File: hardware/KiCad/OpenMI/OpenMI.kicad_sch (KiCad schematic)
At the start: 11 parts, among them Q1 MASTERGAN1, Q2 Q_NMOS_DGS, Q3 Q_NMOS_DGS

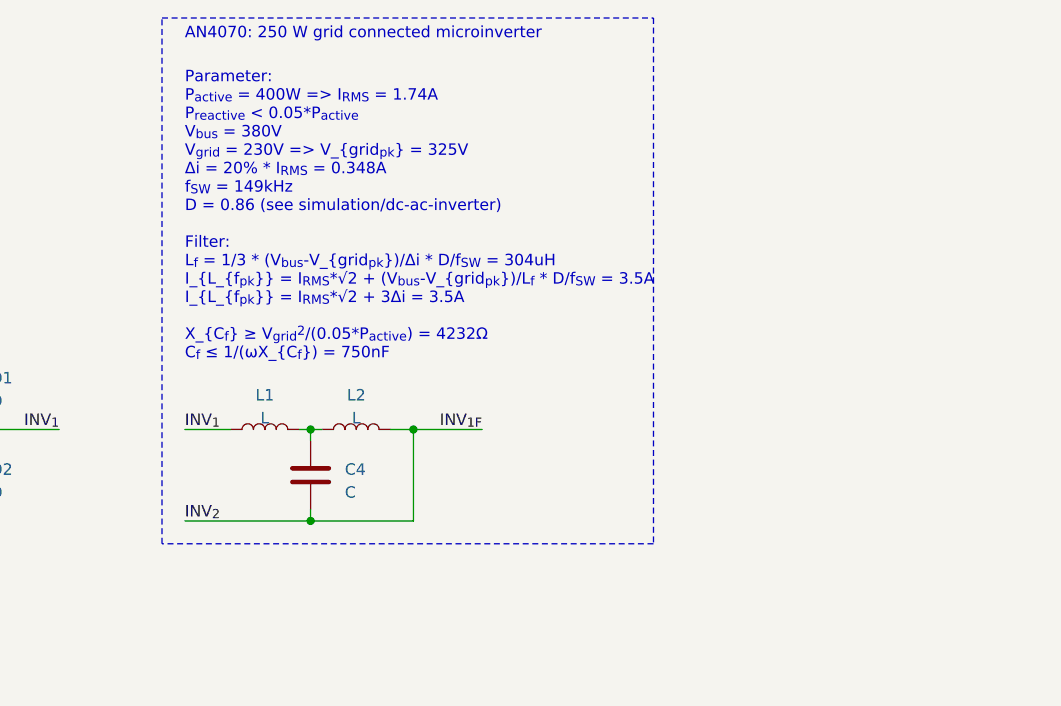
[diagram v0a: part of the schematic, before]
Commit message: hw: Add some possible inductors
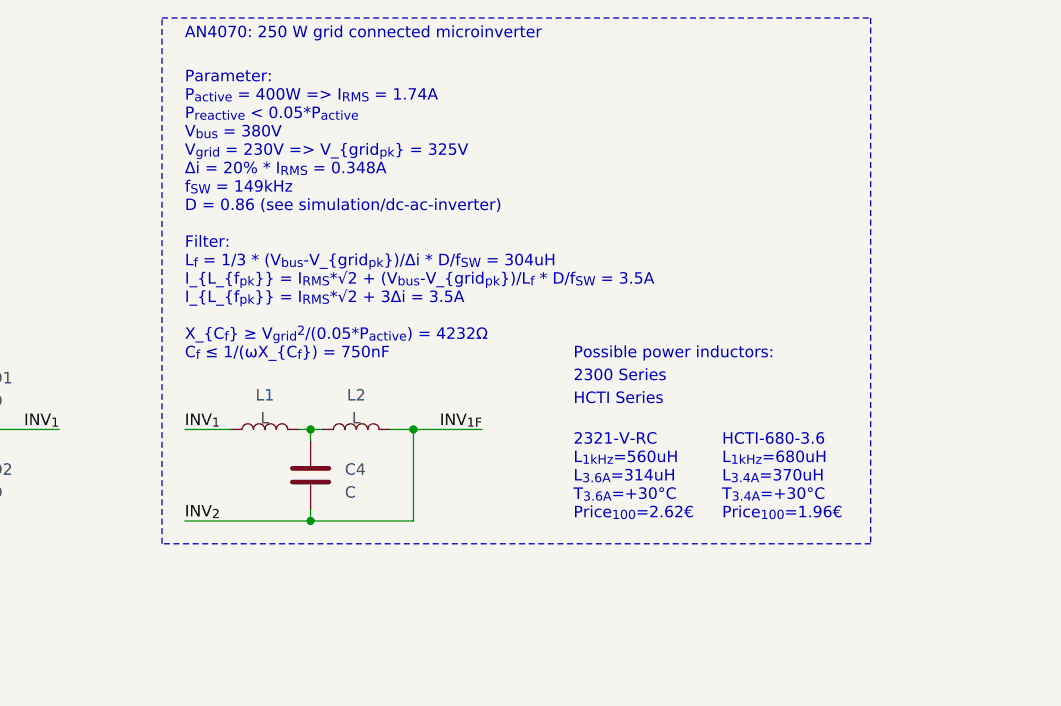
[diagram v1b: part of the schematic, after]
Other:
- note added: "2300 Series"
- note added: "2321-V-RC L_{1kHz}=560uH L_{3.6A}=314uH T_{3.6A}=+30°C Price_{100}=2.62€"
- note added: "HCTI Series"
- note added: "HCTI-680-3.6 L_{1kHz}=680uH L_{3.4A}=370uH T_{3.4A}=+30°C Price_{100}=1.96€"
- note added: "Possible power inductors:"
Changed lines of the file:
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@@
     (stroke (width 0) (type default))
   )
-  (rectangle (start 115.57 26.67) (end 170.18 85.09)
+  (rectangle (start 115.57 26.67) (end 194.31 85.09)
     (stroke (width 0) (type dash))
     (fill (type none))
+  )
+  (text "Possible power inductors:" (at 161.29 64.77 0)
+    (effects (font (size 1.27 1.27)) (justify left bottom))
+  )
+  (text "2321-V-RC \nL_{1kHz}=560uH\nL_{3.6A}=314uH\nT_{3.6A}=+30°C\nPrice_{100}=2.62€"
+    (at 161.29 82.55 0)
+    (effects (font (size 1.27 1.27)) (justify left bottom))
   )
   (text "AN4070: 250 W grid connected microinverter" (at 118.11 29.21 0)
     (effects (font (size 1.27 1.27)) (justify left bottom) (href "https://www.st.com/resource/en/application_note/dm00050692-250-w-grid-connected-microinverter-stmicroelectronics.pdf"))
   )
+  (text "HCTI-680-3.6\nL_{1kHz}=680uH\nL_{3.4A}=370uH\nT_{3.4A}=+30°C\nPrice_{100}=1.96€"
+    (at 177.8 82.55 0)
+    (effects (font (size 1.27 1.27)) (justify left bottom))
+  )
+  (text "HCTI Series" (at 161.29 69.85 0)
+    (effects (font (size 1.27 1.27)) (justify left bottom) (href "https://eu.mouser.com/datasheet/2/643/ds-st-high-current-torodial-inductors-series-1661536.pdf"))
+  )
+  (text "2300 Series" (at 161.29 67.31 0)
+    (effects (font (size 1.27 1.27)) (justify left bottom) (href "https://eu.mouser.com/datasheet/2/54/2300_series-776044.pdf"))
+  )
   (text "Parameter:\nP_{active} = 400W => I_{RMS} = 1.74A\nP_{reactive} < 0.05*P_{active}\nV_{bus} = 380V\nV_{grid} = 230V => V_{grid_{pk}} = 325V\nΔi = 20% * I_{RMS} = 0.348A\nf_{SW} = 149kHz\nD = 0.86 (see simulation/dc-ac-inverter)\n\nFilter:\nL_{f} = 1/3 * (V_{bus}-V_{grid_{pk}})/Δi * D/f_{SW} = 304uH\nI_{L_{f_{pk}}} = I_{RMS}*√2 + (V_{bus}-V_{grid_{pk}})/L_{f} * D/f_{SW} = 3.5A\nI_{L_{f_{pk}}} = I_{RMS}*√2 + 3Δi = 3.5A\n\nX_{C_{f}} ≥ V_{grid}^{2}/(0.05*P_{active}) = 4232Ω\nC_{f} ≤ 1/(ωX_{C_{f}}) = 750nF"

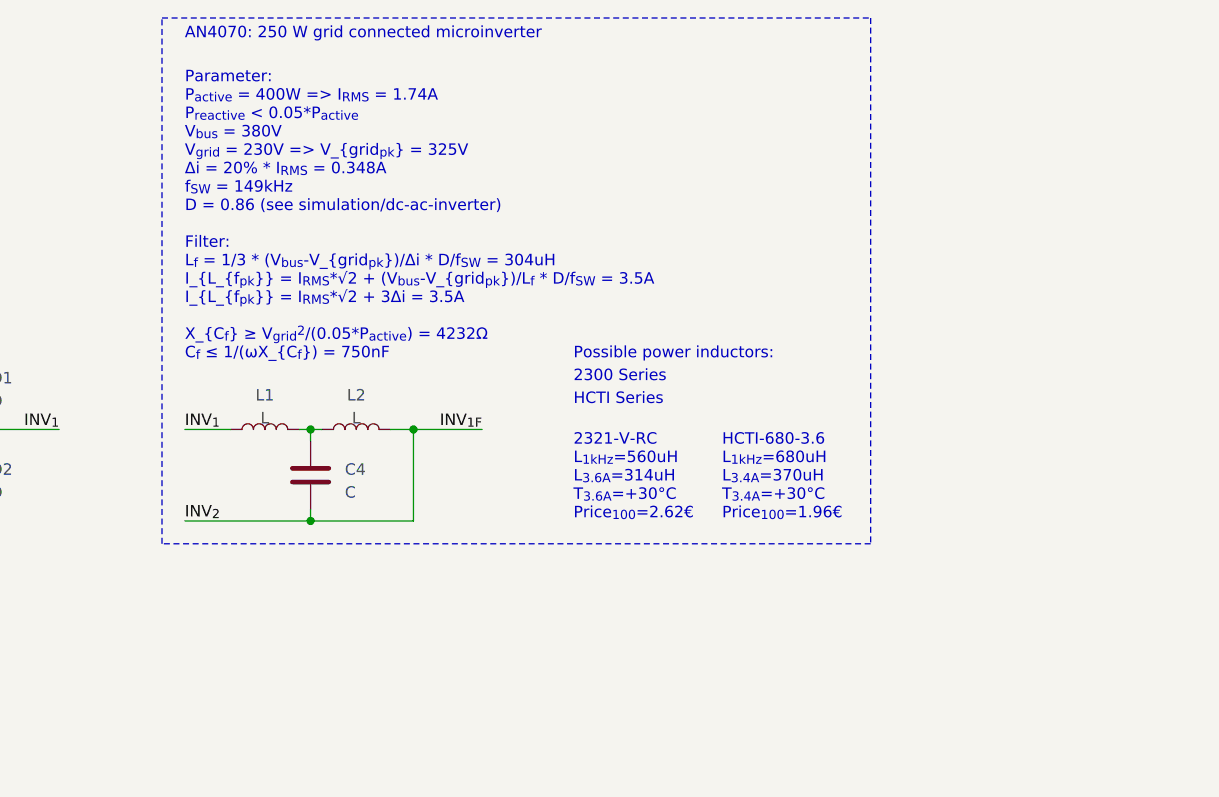
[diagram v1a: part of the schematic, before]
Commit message: hw: fix switching frequency -> update required filter inductance
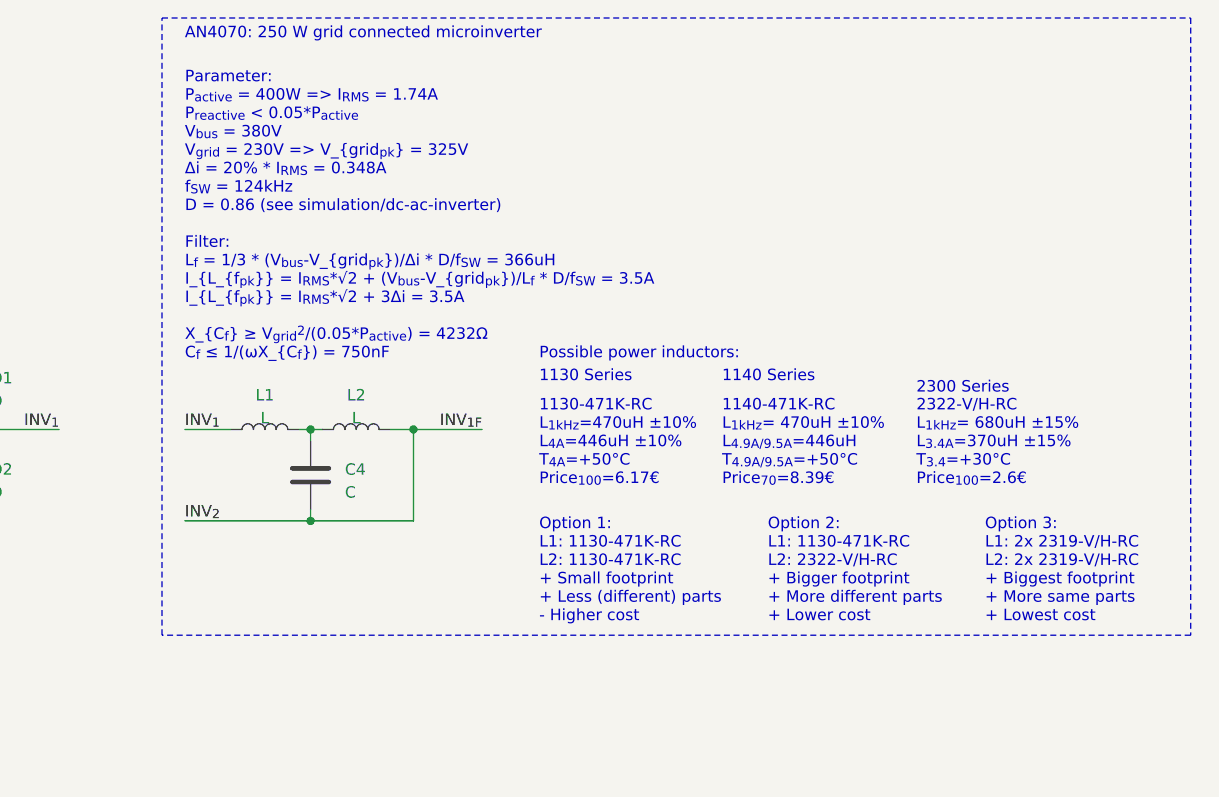
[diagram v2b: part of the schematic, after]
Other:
- note added: "1130 Series"
- note added: "1130-471K-RC L_{1kHz}=470uH ±10% L_{4A}=446uH ±10% T_{4A}=+50°C Price_{100}=6.17€"
- note added: "1140 Series"
- note added: "1140-471K-RC L_{1kHz}= 470uH ±10% L_{4.9A/9.5A}=446uH T_{4.9A/9.5A}=+50°C Price_{70}=8.39€"
- note added: "2322-V/H-RC L_{1kHz}= 680uH ±15% L_{3.4A}=370uH ±15% T_{3.4}=+30°C Price_{100}=2.6€"
- note added: "Option 1: L1: 1130-471K-RC L2: 1130-471K-RC + Small footprint + Less (different) parts - Higher cost"
- note added: "Option 2: L1: 1130-471K-RC L2: 2322-V/H-RC + Bigger footprint + More different parts + Lower cost"
- note added: "Option 3: L1: 2x 2319-V/H-RC L2: 2x 2319-V/H-RC + Biggest footprint + More same parts + Lowest cost"
- note added: "Parameter: P_{active} = 400W => I_{RMS} = 1.74A P_{reactive} < 0.05*P_{active} V_{bus} = 380V V_{grid} = 230V => V_{grid_{pk}} = 325V Δi = 20% * I_{RMS} = 0.348A f_{SW} = 124kHz D = 0.86 (see simulation/dc-ac-inverter) Filter: L_{f} = 1/3 * (V_{bus}-V_{grid_{pk}})/Δi * D/f_{SW} = 366uH I_{L_{f_{pk}}} = I_{RMS}*√2 + (V_{bus}-V_{grid_{pk}})/L_{f} * D/f_{SW} = 3.5A I_{L_{f_{pk}}} = I_{RMS}*√2 + 3Δi 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"
- note removed: "2321-V-RC L_{1kHz}=560uH L_{3.6A}=314uH T_{3.6A}=+30°C Price_{100}=2.62€"
- note removed: "HCTI Series"
- note removed: "HCTI-680-3.6 L_{1kHz}=680uH L_{3.4A}=370uH T_{3.4A}=+30°C Price_{100}=1.96€"
- note removed: "Parameter: P_{active} = 400W => I_{RMS} = 1.74A P_{reactive} < 0.05*P_{active} V_{bus} = 380V V_{grid} = 230V => V_{grid_{pk}} = 325V Δi = 20% * I_{RMS} = 0.348A f_{SW} = 149kHz D = 0.86 (see simulation/dc-ac-inverter) Filter: L_{f} = 1/3 * (V_{bus}-V_{grid_{pk}})/Δi * D/f_{SW} = 304uH I_{L_{f_{pk}}} = I_{RMS}*√2 + (V_{bus}-V_{grid_{pk}})/L_{f} * D/f_{SW} = 3.5A I_{L_{f_{pk}}} = I_{RMS}*√2 + 3Δi 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"
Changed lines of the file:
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@@
     (stroke (width 0) (type default))
   )
-  (rectangle (start 115.57 26.67) (end 194.31 85.09)
+  (rectangle (start 115.57 26.67) (end 229.87 95.25)
     (stroke (width 0) (type dash))
     (fill (type none))
   )
-  (text "Possible power inductors:" (at 161.29 64.77 0)
+  (text "Option 1:\nL1: 1130-471K-RC\nL2: 1130-471K-RC\n+ Small footprint\n+ Less (different) parts\n- Higher cost"
+    (at 157.48 93.98 0)
     (effects (font (size 1.27 1.27)) (justify left bottom))
   )
-  (text "2321-V-RC \nL_{1kHz}=560uH\nL_{3.6A}=314uH\nT_{3.6A}=+30°C\nPrice_{100}=2.62€"
-    (at 161.29 82.55 0)
+  (text "Possible power inductors:" (at 157.48 64.77 0)
+    (effects (font (size 1.27 1.27)) (justify left bottom))
+  )
+  (text "1130-471K-RC \nL_{1kHz}=470uH ±10%\nL_{4A}=446uH ±10%\nT_{4A}=+50°C\nPrice_{100}=6.17€"
+    (at 157.48 78.74 0)
     (effects (font (size 1.27 1.27)) (justify left bottom))
   )
@@
     (effects (font (size 1.27 1.27)) (justify left bottom) (href "https://www.st.com/resource/en/application_note/dm00050692-250-w-grid-connected-microinverter-stmicroelectronics.pdf"))
   )
-  (text "HCTI-680-3.6\nL_{1kHz}=680uH\nL_{3.4A}=370uH\nT_{3.4A}=+30°C\nPrice_{100}=1.96€"
-    (at 177.8 82.55 0)
+  (text "1140-471K-RC\nL_{1kHz}= 470uH ±10% \nL_{4.9A/9.5A}=446uH\nT_{4.9A/9.5A}=+50°C\nPrice_{70}=8.39€"
+    (at 177.8 78.74 0)
     (effects (font (size 1.27 1.27)) (justify left bottom))
   )
-  (text "HCTI Series" (at 161.29 69.85 0)
-    (effects (font (size 1.27 1.27)) (justify left bottom) (href "https://eu.mouser.com/datasheet/2/643/ds-st-high-current-torodial-inductors-series-1661536.pdf"))
+  (text "2300 Series" (at 199.39 68.58 0)
+    (effects (font (size 1.27 1.27)) (justify left bottom) (href "https://www.bourns.com/docs/product-datasheets/2300_series.pdf"))
   )
-  (text "2300 Series" (at 161.29 67.31 0)
-    (effects (font (size 1.27 1.27)) (justify left bottom) (href "https://eu.mouser.com/datasheet/2/54/2300_series-776044.pdf"))
+  (text "1140 Series" (at 177.8 67.31 0)
+    (effects (font (size 1.27 1.27)) (justify left bottom) (href "https://www.bourns.com/docs/product-datasheets/1140_series.pdf"))
   )
-  (text "Parameter:\nP_{active} = 400W => I_{RMS} = 1.74A\nP_{reactive} < 0.05*P_{active}\nV_{bus} = 380V\nV_{grid} = 230V => V_{grid_{pk}} = 325V\nΔi = 20% * I_{RMS} = 0.348A\nf_{SW} = 149kHz\nD = 0.86 (see simulation/dc-ac-inverter)\n\nFilter:\nL_{f} = 1/3 * (V_{bus}-V_{grid_{pk}})/Δi * D/f_{SW} = 304uH\nI_{L_{f_{pk}}} = I_{RMS}*√2 + (V_{bus}-V_{grid_{pk}})/L_{f} * D/f_{SW} = 3.5A\nI_{L_{f_{pk}}} = I_{RMS}*√2 + 3Δi = 3.5A\n\nX_{C_{f}} ≥ V_{grid}^{2}/(0.05*P_{active}) = 4232Ω\nC_{f} ≤ 1/(ωX_{C_{f}}) = 750nF"
+  (text "1130 Series" (at 157.48 67.31 0)
+    (effects (font (size 1.27 1.27)) (justify left bottom) (href "https://www.bourns.com/docs/product-datasheets/1130_series.pdf"))
+  )
+  (text "2322-V/H-RC\nL_{1kHz}= 680uH ±15% \nL_{3.4A}=370uH ±15% \nT_{3.4}=+30°C\nPrice_{100}=2.6€"
+    (at 199.39 78.74 0)
+    (effects (font (size 1.27 1.27)) (justify left bottom))
+  )
+  (text "Option 2:\nL1: 1130-471K-RC\nL2: 2322-V/H-RC\n+ Bigger footprint\n+ More different parts\n+ Lower cost"
+    (at 182.88 93.98 0)
+    (effects (font (size 1.27 1.27)) (justify left bottom))
+  )
+  (text "Parameter:\nP_{active} = 400W => I_{RMS} = 1.74A\nP_{reactive} < 0.05*P_{active}\nV_{bus} = 380V\nV_{grid} = 230V => V_{grid_{pk}} = 325V\nΔi = 20% * I_{RMS} = 0.348A\nf_{SW} = 124kHz\nD = 0.86 (see simulation/dc-ac-inverter)\n\nFilter:\nL_{f} = 1/3 * (V_{bus}-V_{grid_{pk}})/Δi * D/f_{SW} = 366uH\nI_{L_{f_{pk}}} = I_{RMS}*√2 + (V_{bus}-V_{grid_{pk}})/L_{f} * D/f_{SW} = 3.5A\nI_{L_{f_{pk}}} = I_{RMS}*√2 + 3Δi = 3.5A\n\nX_{C_{f}} ≥ V_{grid}^{2}/(0.05*P_{active}) = 4232Ω\nC_{f} ≤ 1/(ωX_{C_{f}}) = 750nF"
     (at 118.11 64.77 0)
     (effects (font (size 1.27 1.27)) (justify left bottom))
   )
+  (text "Option 3:\nL1: 2x 2319-V/H-RC\nL2: 2x 2319-V/H-RC\n+ Biggest footprint\n+ More same parts\n+ Lowest cost"
+    (at 207.01 93.98 0)
+    (effects (font (size 1.27 1.27)) (justify left bottom))
+  )

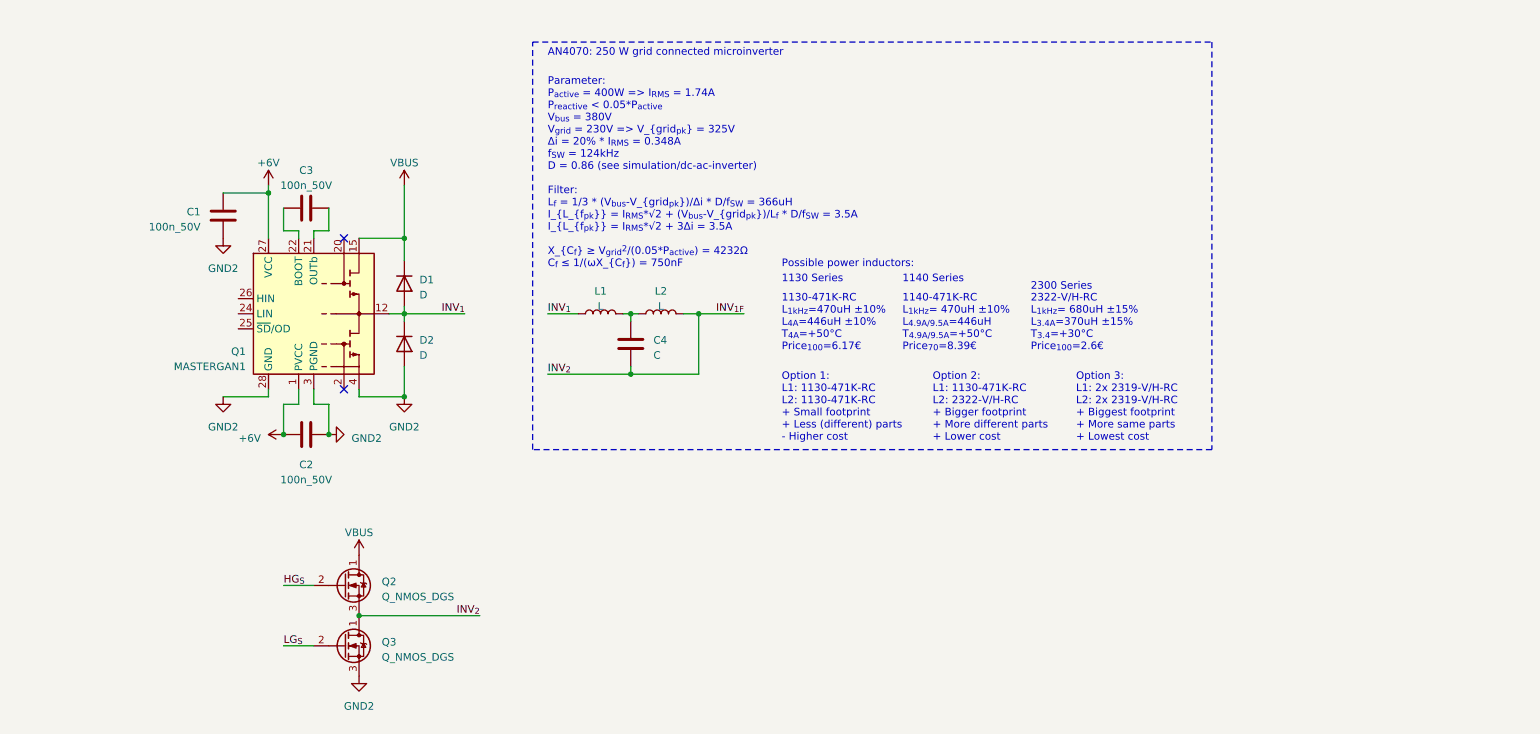
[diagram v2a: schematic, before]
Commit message: hw: Add dc bus power decoupling capacitors
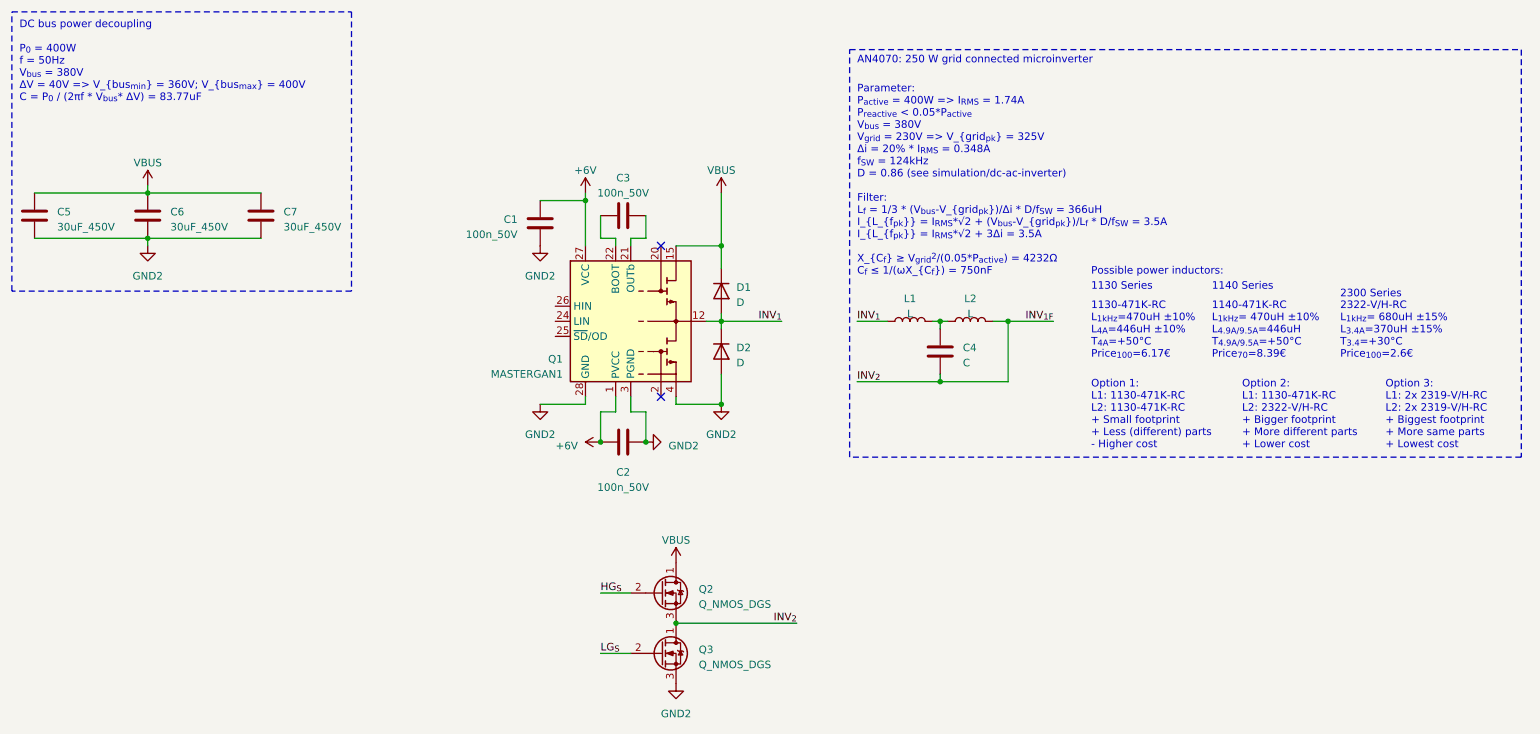
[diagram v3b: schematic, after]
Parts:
- added C5, C6, C7: 30uF_450V, OpenCE:C_Rect_L43mm_W42mm_H25mm_P37.5mm_P20.3mm_KEMET, symbol _C_Film:30uF_450V
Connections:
- net GND: now also C5.2, C6.2, C7.2
- net VBUS: now also C5.1, C6.1, C7.1
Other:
- note added: "DC bus power decoupling P_{0} = 400W f = 50Hz V_{bus} = 380V ΔV = 40V => V_{bus_{min}} = 360V; V_{bus_{max}} = 400V C = P_{0} / (2πf * V_{bus}* ΔV) = 83.77uF"
- moved on the sheet: C1, C2, C3, C4, D1, D2, L1, L2, Q1, Q2, Q3
